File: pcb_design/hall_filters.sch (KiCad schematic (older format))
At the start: 8 parts

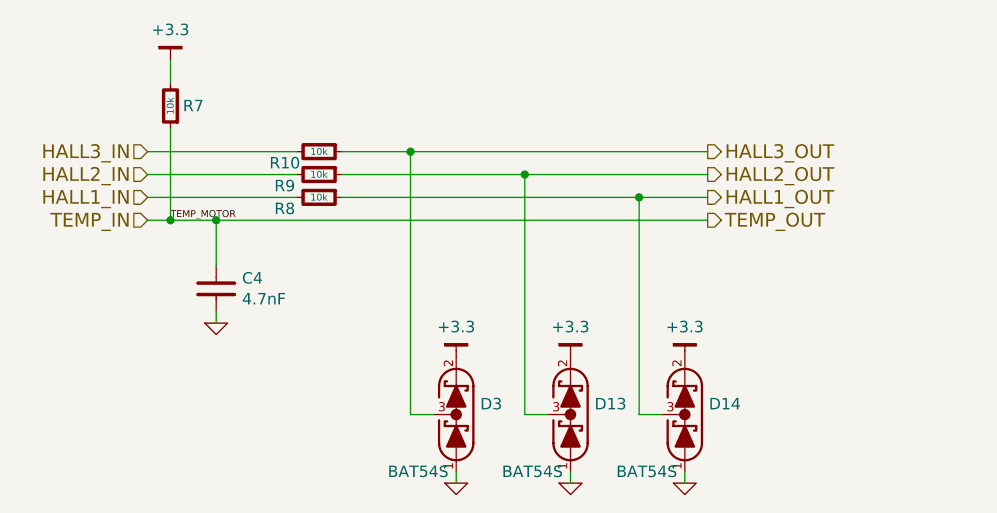
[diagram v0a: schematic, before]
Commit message: Added reverse polarity protection on the isolated side of CON connector. Also, more layout
Signed-off-by: Marcos Chaparro <mchaparro@paltatech.com>
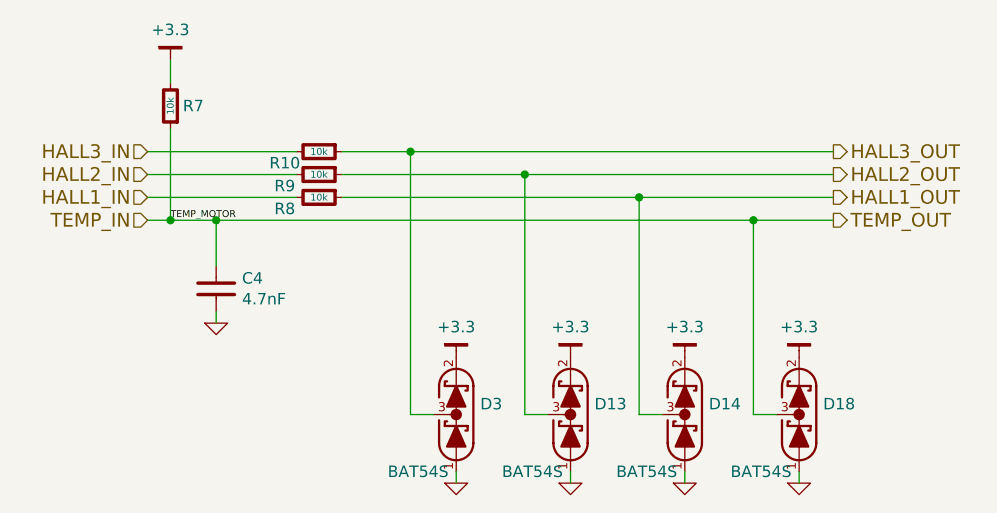
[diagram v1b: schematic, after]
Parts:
- added D18: BAT54S, smd-semi:SOT-23, symbol BAT54S
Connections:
- net +3.3: now also D18.2 (K)
- net GND: now also D18.1 (A)
- net TEMP_IN: now also D18.3 (COM)
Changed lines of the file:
@@
 $EndDescr
 $Comp
-L GND-RESCUE-BLDC_4 #PWR036
+L GND-RESCUE-BLDC_4 #PWR37
 U 1 1 53FBB5D4
 P 5100 4300
-F 0 "#PWR036" H 5100 4300 30  0001 C CNN
+F 0 "#PWR37" H 5100 4300 30  0001 C CNN
 F 1 "GND" H 5100 4230 30  0001 C CNN
 F 2 "" H 5100 4300 60  0001 C CNN
@@
 Text HLabel 4800 3850 0    60   Input ~ 0
 TEMP_IN
-Text HLabel 7250 3550 2    60   Output ~ 0
+Text HLabel 7800 3550 2    60   Output ~ 0
 HALL3_OUT
-Text HLabel 7250 3650 2    60   Output ~ 0
+Text HLabel 7800 3650 2    60   Output ~ 0
 HALL2_OUT
-Text HLabel 7250 3750 2    60   Output ~ 0
+Text HLabel 7800 3750 2    60   Output ~ 0
 HALL1_OUT
-Text HLabel 7250 3850 2    60   Output ~ 0
+Text HLabel 7800 3850 2    60   Output ~ 0
 TEMP_OUT
 $Comp
@@
 $EndComp
 $Comp
-L GND-RESCUE-BLDC_4 #PWR037
+L GND-RESCUE-BLDC_4 #PWR39
 U 1 1 588A8030
 P 6150 5000
-F 0 "#PWR037" H 6150 5000 30  0001 C CNN
+F 0 "#PWR39" H 6150 5000 30  0001 C CNN
 F 1 "GND" H 6150 4930 30  0001 C CNN
 F 2 "" H 6150 5000 60  0001 C CNN
@@
 	4800 3550 5450 3550
 Wire Wire Line
-	5650 3750 7250 3750
-Wire Wire Line
-	5650 3650 7250 3650
+	5650 3750 7800 3750
+Wire Wire Line
+	5650 3650 7800 3650
 Wire Wire Line
 	5950 3550 5950 4700
 Wire Wire Line
-	5650 3550 7250 3550
+	5650 3550 7800 3550
 Wire Wire Line
 	5100 3850 5100 4050
@@
 	4900 3150 4900 3250
 Wire Wire Line
-	4800 3850 7250 3850
+	4800 3850 7800 3850
 Connection ~ 5100 3850
 Wire Wire Line
@@
 $EndComp
 $Comp
-L GND-RESCUE-BLDC_4 #PWR038
+L GND-RESCUE-BLDC_4 #PWR41
 U 1 1 588A8431
 P 6650 5000
-F 0 "#PWR038" H 6650 5000 30  0001 C CNN
+F 0 "#PWR41" H 6650 5000 30  0001 C CNN
 F 1 "GND" H 6650 4930 30  0001 C CNN
 F 2 "" H 6650 5000 60  0001 C CNN
@@
 $EndComp
 $Comp
-L GND-RESCUE-BLDC_4 #PWR039
+L GND-RESCUE-BLDC_4 #PWR43
 U 1 1 588A87E2
 P 7150 5000
-F 0 "#PWR039" H 7150 5000 30  0001 C CNN
+F 0 "#PWR43" H 7150 5000 30  0001 C CNN
 F 1 "GND" H 7150 4930 30  0001 C CNN
 F 2 "" H 7150 5000 60  0001 C CNN
@@
 	5100 4300 5100 4250
 $Comp
-L +3.3 #PWR040
+L +3.3 #PWR36
 U 1 1 588B84F4
 P 4900 3150
-F 0 "#PWR040" H 0   100 30  0001 C CNN
+F 0 "#PWR36" H 0   100 30  0001 C CNN
 F 1 "+3.3" H 4900 3283 50  0000 C CNN
 F 2 "" H 0   50  60  0000 C CNN
@@
 $EndComp
 $Comp
-L +3.3 #PWR041
+L +3.3 #PWR38
 U 1 1 588B856B
 P 6150 4450
-F 0 "#PWR041" H 6200 4500 30  0001 C CNN
+F 0 "#PWR38" H 6200 4500 30  0001 C CNN
 F 1 "+3.3" H 6150 4583 50  0000 C CNN
 F 2 "" H -300 100 60  0000 C CNN
@@
 $EndComp
 $Comp
-L +3.3 #PWR042
+L +3.3 #PWR40
 U 1 1 588B8595
 P 6650 4450
-F 0 "#PWR042" H 6700 4500 30  0001 C CNN
+F 0 "#PWR40" H 6700 4500 30  0001 C CNN
 F 1 "+3.3" H 6650 4583 50  0000 C CNN
 F 2 "" H 200 100 60  0000 C CNN
@@
 $EndComp
 $Comp
-L +3.3 #PWR043
+L +3.3 #PWR42
 U 1 1 588B85B8
 P 7150 4450
-F 0 "#PWR043" H 7200 4500 30  0001 C CNN
+F 0 "#PWR42" H 7200 4500 30  0001 C CNN
 F 1 "+3.3" H 7150 4583 50  0000 C CNN
 F 2 "" H 700 100 60  0000 C CNN
@@
 	1    0    0    -1
 $EndComp
+$Comp
+L BAT54S D18
+U 1 1 588F7B43
+P 7650 4700
+F 0 "D18" V 7696 4595 50  0000 R CNN
+F 1 "BAT54S" V 7400 5000 50  0000 R CNN
+F 2 "smd-semi:SOT-23" H 7650 4550 60  0001 C CNN
+F 3 "" V 7600 4700 60  0000 C CNN
+F 4 "SCHOTTKY BAT54S" H 7650 4450 60  0001 C CNN "BOM"
+	1    7650 4700
+	0    -1   -1   0
+$EndComp
+$Comp
+L +3.3 #PWR44
+U 1 1 588F7C22
+P 7650 4450
+F 0 "#PWR44" H 7700 4500 30  0001 C CNN
+F 1 "+3.3" H 7650 4583 50  0000 C CNN
+F 2 "" H 1200 100 60  0000 C CNN
+F 3 "" H 1200 100 60  0000 C CNN
+	1    7650 4450
+	1    0    0    -1
+$EndComp
+$Comp
+L GND-RESCUE-BLDC_4 #PWR45
+U 1 1 588F7C48
+P 7650 5000
+F 0 "#PWR45" H 7650 5000 30  0001 C CNN
+F 1 "GND" H 7650 4930 30  0001 C CNN
+F 2 "" H 7650 5000 60  0001 C CNN
+F 3 "" H 7650 5000 60  0001 C CNN
+	1    7650 5000
+	1    0    0    -1
+$EndComp
+Wire Wire Line
+	7650 5000 7650 4950
+Wire Wire Line
+	7550 4700 7450 4700
+Wire Wire Line
+	7450 4700 7450 3850
+Connection ~ 7450 3850
 $EndSCHEMATC

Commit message: Updated component values according to simulations. 1.5khz for user inputs and  240khz lp pass filters for motor control
Signed-off-by: Marcos Chaparro <mchaparro@paltatech.com>
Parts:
- C4: BOM CAP MLCC 100pF C0G 50V 5% [0603] -> CAP MLCC 4.7nF X7R 50V 10% [0603]; mfg# (none) -> GRM188R71H472KA01D
- D13, D14, D18, D3: mfg# (none) -> TBAT54S,LM
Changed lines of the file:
@@
 F 2 "smd-semi:SOT-23" H 6150 4550 60  0001 C CNN
 F 3 "" V 6100 4700 60  0000 C CNN
-F 4 "SCHOTTKY BAT54S" H 6150 4450 60  0001 C CNN "BOM"
+F 4 "TBAT54S,LM" H 6150 4700 60  0001 C CNN "mfg#"
+F 5 "SCHOTTKY BAT54S" H 6150 4450 60  0001 C CNN "BOM"
 	1    6150 4700
 	0    -1   -1   0
@@
 F 2 "smd-semi:SOT-23" H 6650 4550 60  0001 C CNN
 F 3 "" V 6600 4700 60  0000 C CNN
-F 4 "SCHOTTKY BAT54S" H 6650 4450 60  0001 C CNN "BOM"
+F 4 "TBAT54S,LM" H 6650 4700 60  0001 C CNN "mfg#"
+F 5 "SCHOTTKY BAT54S" H 6650 4450 60  0001 C CNN "BOM"
 	1    6650 4700
 	0    -1   -1   0
@@
 F 2 "smd-semi:SOT-23" H 7150 4550 60  0001 C CNN
 F 3 "" V 7100 4700 60  0000 C CNN
-F 4 "SCHOTTKY BAT54S" H 7150 4450 60  0001 C CNN "BOM"
+F 4 "TBAT54S,LM" H 7150 4700 60  0001 C CNN "mfg#"
+F 5 "SCHOTTKY BAT54S" H 7150 4450 60  0001 C CNN "BOM"
 	1    7150 4700
 	0    -1   -1   0
@@
 F 2 "IPC7351-Nominal:CAPC1608X55" H 5100 4150 50  0001 C CNN
 F 3 "" H 5090 4125 60  0000 C CNN
-F 4 "CAP MLCC 100pF C0G 50V 5% [0603]" H 5900 4700 60  0001 C CNN "BOM"
+F 4 "GRM188R71H472KA01D" H 5100 4150 60  0001 C CNN "mfg#"
+F 5 "CAP MLCC 4.7nF X7R 50V 10% [0603]" H 5900 4700 60  0001 C CNN "BOM"
 	1    5100 4150
 	1    0    0    -1
@@
 F 2 "smd-semi:SOT-23" H 7650 4550 60  0001 C CNN
 F 3 "" V 7600 4700 60  0000 C CNN
-F 4 "SCHOTTKY BAT54S" H 7650 4450 60  0001 C CNN "BOM"
+F 4 "TBAT54S,LM" H 7650 4700 60  0001 C CNN "mfg#"
+F 5 "SCHOTTKY BAT54S" H 7650 4450 60  0001 C CNN "BOM"
 	1    7650 4700
 	0    -1   -1   0

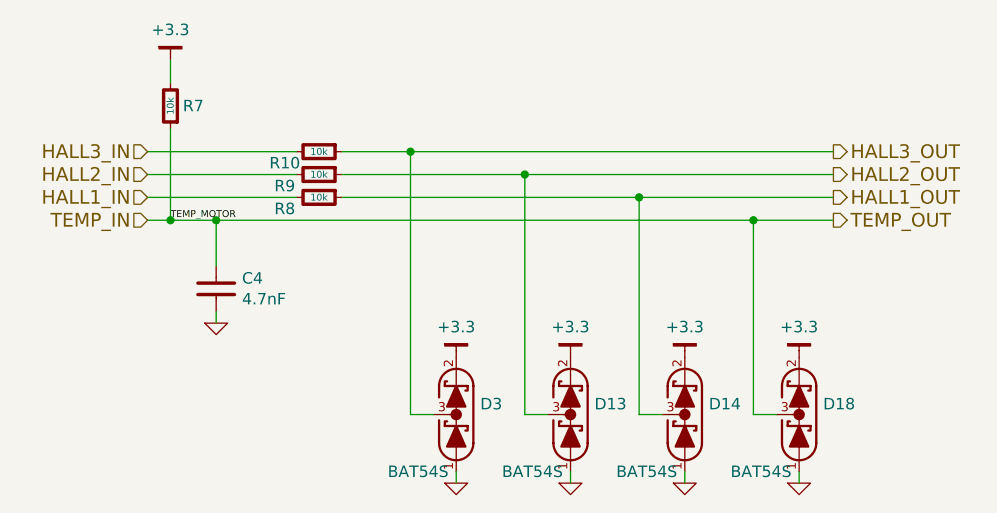
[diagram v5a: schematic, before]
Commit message: Completed some part numbers
Signed-off-by: Marcos Chaparro <mchaparro@paltatech.com>
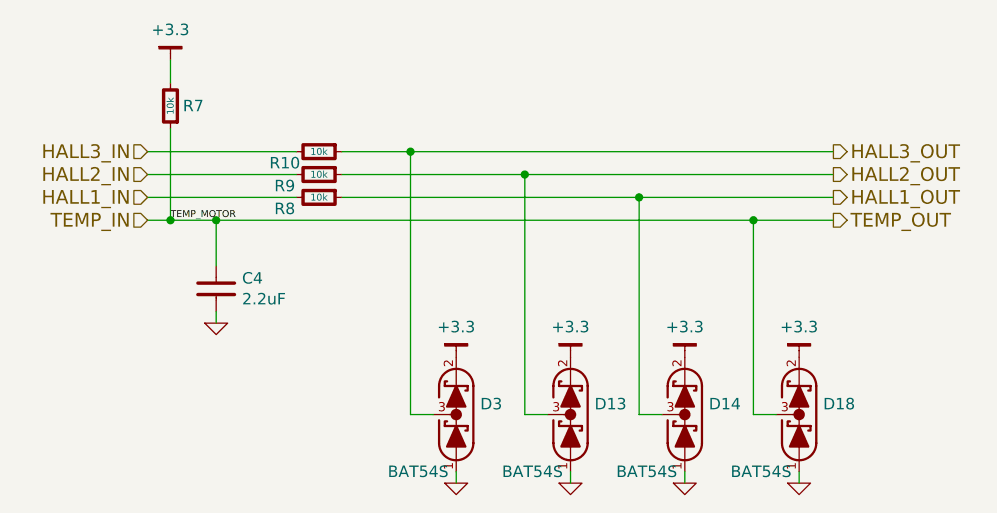
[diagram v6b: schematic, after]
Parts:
- C4: value 4.7nF -> 2.2uF; MFR (none) -> Murata Electronics North America; MPN (none) -> GRM188R71A225KE15D; SPN (none) -> 490-4520-1-ND; SPR (none) -> Digikey

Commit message: Completed part number, manufacturer, etc fields. Simulated analog conditioning
Signed-off-by: Marcos Chaparro <mchaparro@paltatech.com>
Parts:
- D13, D14, D18, D3: MFR (none) -> Toshiba Semiconductor and Storage; MPN (none) -> TBAT54S,LM; SPN (none) -> TBAT54SLMCT-ND; SPR (none) -> Digikey
- R10, R7, R8, R9: MFR (none) -> Yageo; MPN (none) -> RC0603FR-0710KL; SPN (none) -> 311-10.0KHRCT-ND; SPR (none) -> Digikey
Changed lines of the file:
@@
 F 1 "BAT54S" V 5900 5000 50 0000 R CNN
 F 2 "smd-semi:SOT-23" H 6150 4550 60 0001 C CNN
-F 3 "" V 6100 4700 60 0000 C CNN
+F 3 "http://toshiba.semicon-storage.com/info/docget.jsp?did=37137&prodName=TBAT54" V 6100 4700 60 0001 C CNN
 F 4 "TBAT54S,LM" H 6150 4700 60 0001 C CNN "mfg#"
 F 5 "SCHOTTKY BAT54S" H 6150 4450 60 0001 C CNN "BOM"
-F 6 "" H 0 0 50 0001 C CNN "MFR"
-F 7 "" H 0 0 50 0001 C CNN "MPN"
-F 8 "" H 0 0 50 0001 C CNN "SPR"
-F 9 "" H 0 0 50 0001 C CNN "SPN"
+F 6 "Toshiba Semiconductor and Storage" H 0 0 50 0001 C CNN "MFR"
+F 7 "TBAT54S,LM" H 0 0 50 0001 C CNN "MPN"
+F 8 "Digikey" H 0 0 50 0001 C CNN "SPR"
+F 9 "TBAT54SLMCT-ND" H 0 0 50 0001 C CNN "SPN"
 F 10 "" H 0 0 50 0001 C CNN "SPURL"
 	1    6150 4700
@@
 F 1 "BAT54S" V 6400 5000 50 0000 R CNN
 F 2 "smd-semi:SOT-23" H 6650 4550 60 0001 C CNN
-F 3 "" V 6600 4700 60 0000 C CNN
+F 3 "http://toshiba.semicon-storage.com/info/docget.jsp?did=37137&prodName=TBAT54" V 6600 4700 60 0001 C CNN
 F 4 "TBAT54S,LM" H 6650 4700 60 0001 C CNN "mfg#"
 F 5 "SCHOTTKY BAT54S" H 6650 4450 60 0001 C CNN "BOM"
-F 6 "" H 0 0 50 0001 C CNN "MFR"
-F 7 "" H 0 0 50 0001 C CNN "MPN"
-F 8 "" H 0 0 50 0001 C CNN "SPR"
-F 9 "" H 0 0 50 0001 C CNN "SPN"
+F 6 "Toshiba Semiconductor and Storage" H 0 0 50 0001 C CNN "MFR"
+F 7 "TBAT54S,LM" H 0 0 50 0001 C CNN "MPN"
+F 8 "Digikey" H 0 0 50 0001 C CNN "SPR"
+F 9 "TBAT54SLMCT-ND" H 0 0 50 0001 C CNN "SPN"
 F 10 "" H 0 0 50 0001 C CNN "SPURL"
 	1    6650 4700
@@
 F 1 "BAT54S" V 6900 5000 50 0000 R CNN
 F 2 "smd-semi:SOT-23" H 7150 4550 60 0001 C CNN
-F 3 "" V 7100 4700 60 0000 C CNN
+F 3 "http://toshiba.semicon-storage.com/info/docget.jsp?did=37137&prodName=TBAT54" V 7100 4700 60 0001 C CNN
 F 4 "TBAT54S,LM" H 7150 4700 60 0001 C CNN "mfg#"
 F 5 "SCHOTTKY BAT54S" H 7150 4450 60 0001 C CNN "BOM"
-F 6 "" H 0 0 50 0001 C CNN "MFR"
-F 7 "" H 0 0 50 0001 C CNN "MPN"
-F 8 "" H 0 0 50 0001 C CNN "SPR"
-F 9 "" H 0 0 50 0001 C CNN "SPN"
+F 6 "Toshiba Semiconductor and Storage" H 0 0 50 0001 C CNN "MFR"
+F 7 "TBAT54S,LM" H 0 0 50 0001 C CNN "MPN"
+F 8 "Digikey" H 0 0 50 0001 C CNN "SPR"
+F 9 "TBAT54SLMCT-ND" H 0 0 50 0001 C CNN "SPN"
 F 10 "" H 0 0 50 0001 C CNN "SPURL"
 	1    7150 4700
@@
 F 1 "10k" V 5550 3550 30 0000 C CNN
 F 2 "IPC7351-Nominal:RESC1608X50" H 5550 3550 50 0001 C CNN
-F 3 "" H 5550 3600 60 0000 C CNN
+F 3 "" H 5550 3600 60 0001 C CNN
 F 4 "RES SMD 1k 5% [0603]" H 6300 4100 60 0001 C CNN "BOM"
-F 5 "" H 0 0 50 0001 C CNN "MFR"
-F 6 "" H 0 0 50 0001 C CNN "MPN"
-F 7 "" H 0 0 50 0001 C CNN "SPR"
-F 8 "" H 0 0 50 0001 C CNN "SPN"
+F 5 "Yageo" H 0 0 50 0001 C CNN "MFR"
+F 6 "RC0603FR-0710KL" H 0 0 50 0001 C CNN "MPN"
+F 7 "Digikey" H 0 0 50 0001 C CNN "SPR"
+F 8 "311-10.0KHRCT-ND" H 0 0 50 0001 C CNN "SPN"
 F 9 "" H 0 0 50 0001 C CNN "SPURL"
 	1    5550 3550
@@
 F 1 "10k" V 5550 3650 30 0000 C CNN
 F 2 "IPC7351-Nominal:RESC1608X50" H 5550 3650 50 0001 C CNN
-F 3 "" H 5550 3700 60 0000 C CNN
+F 3 "" H 5550 3700 60 0001 C CNN
 F 4 "RES SMD 1k 5% [0603]" H 6300 4200 60 0001 C CNN "BOM"
-F 5 "" H 0 0 50 0001 C CNN "MFR"
-F 6 "" H 0 0 50 0001 C CNN "MPN"
-F 7 "" H 0 0 50 0001 C CNN "SPR"
-F 8 "" H 0 0 50 0001 C CNN "SPN"
+F 5 "Yageo" H 0 0 50 0001 C CNN "MFR"
+F 6 "RC0603FR-0710KL" H 0 0 50 0001 C CNN "MPN"
+F 7 "Digikey" H 0 0 50 0001 C CNN "SPR"
+F 8 "311-10.0KHRCT-ND" H 0 0 50 0001 C CNN "SPN"
 F 9 "" H 0 0 50 0001 C CNN "SPURL"
 	1    5550 3650
@@
 F 1 "10k" V 5550 3750 30 0000 C CNN
 F 2 "IPC7351-Nominal:RESC1608X50" H 5550 3750 50 0001 C CNN
-F 3 "" H 5550 3800 60 0000 C CNN
+F 3 "" H 5550 3800 60 0001 C CNN
 F 4 "RES SMD 1k 5% [0603]" H 6300 4300 60 0001 C CNN "BOM"
-F 5 "" H 0 0 50 0001 C CNN "MFR"
-F 6 "" H 0 0 50 0001 C CNN "MPN"
-F 7 "" H 0 0 50 0001 C CNN "SPR"
-F 8 "" H 0 0 50 0001 C CNN "SPN"
+F 5 "Yageo" H 0 0 50 0001 C CNN "MFR"
+F 6 "RC0603FR-0710KL" H 0 0 50 0001 C CNN "MPN"
+F 7 "Digikey" H 0 0 50 0001 C CNN "SPR"
+F 8 "311-10.0KHRCT-ND" H 0 0 50 0001 C CNN "SPN"
 F 9 "" H 0 0 50 0001 C CNN "SPURL"
 	1    5550 3750
@@
 F 1 "10k" V 4900 3350 30 0000 C CNN
 F 2 "IPC7351-Nominal:RESC1608X50" H 4900 3350 50 0001 C CNN
-F 3 "" H 4900 3400 60 0000 C CNN
+F 3 "" H 4900 3400 60 0001 C CNN
 F 4 "RES SMD 1k 5% [0603]" H 5650 3900 60 0001 C CNN "BOM"
-F 5 "" H 0 0 50 0001 C CNN "MFR"
-F 6 "" H 0 0 50 0001 C CNN "MPN"
-F 7 "" H 0 0 50 0001 C CNN "SPR"
-F 8 "" H 0 0 50 0001 C CNN "SPN"
+F 5 "Yageo" H 0 0 50 0001 C CNN "MFR"
+F 6 "RC0603FR-0710KL" H 0 0 50 0001 C CNN "MPN"
+F 7 "Digikey" H 0 0 50 0001 C CNN "SPR"
+F 8 "311-10.0KHRCT-ND" H 0 0 50 0001 C CNN "SPN"
 F 9 "" H 0 0 50 0001 C CNN "SPURL"
 	1    4900 3350
@@
 F 1 "BAT54S" V 7400 5000 50 0000 R CNN
 F 2 "smd-semi:SOT-23" H 7650 4550 60 0001 C CNN
-F 3 "" V 7600 4700 60 0000 C CNN
+F 3 "http://toshiba.semicon-storage.com/info/docget.jsp?did=37137&prodName=TBAT54" V 7600 4700 60 0001 C CNN
 F 4 "TBAT54S,LM" H 7650 4700 60 0001 C CNN "mfg#"
 F 5 "SCHOTTKY BAT54S" H 7650 4450 60 0001 C CNN "BOM"
-F 6 "" H 0 0 50 0001 C CNN "MFR"
-F 7 "" H 0 0 50 0001 C CNN "MPN"
-F 8 "" H 0 0 50 0001 C CNN "SPR"
-F 9 "" H 0 0 50 0001 C CNN "SPN"
+F 6 "Toshiba Semiconductor and Storage" H 0 0 50 0001 C CNN "MFR"
+F 7 "TBAT54S,LM" H 0 0 50 0001 C CNN "MPN"
+F 8 "Digikey" H 0 0 50 0001 C CNN "SPR"
+F 9 "TBAT54SLMCT-ND" H 0 0 50 0001 C CNN "SPN"
 F 10 "" H 0 0 50 0001 C CNN "SPURL"
 	1    7650 4700
